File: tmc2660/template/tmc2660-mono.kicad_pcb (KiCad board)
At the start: 4 copper layers, 25 x 40 mm, 19 parts, among them J100 0R, M100 Mount, M101 Mount, P100 Motor, U100 TMC2660

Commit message: Consistently name first block TMC2660-100 in schematic and pcb.
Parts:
- removed REF**: OSHW, Symbols:Symbol_OSHW-Logo_SilkScreen
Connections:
- net /TMC2660-Block/A1 renamed /TMC2660-100/A1
- net /TMC2660-Block/A2 renamed /TMC2660-100/A2
- net /TMC2660-Block/B1 renamed /TMC2660-100/B1
- net /TMC2660-Block/B2 renamed /TMC2660-100/B2
- net /TMC2660-Block/BRA renamed /TMC2660-100/BRA
- net /TMC2660-Block/BRB renamed /TMC2660-100/BRB
- net /TMC2660-Block/CS renamed /TMC2660-100/CS
- net /TMC2660-Block/DIR renamed /TMC2660-100/DIR
- net /TMC2660-Block/GLOBAL_MISO renamed /TMC2660-100/GLOBAL_MISO
- net /TMC2660-Block/MISO renamed /TMC2660-100/MISO
- net /TMC2660-Block/MOSI renamed /TMC2660-100/MOSI
- net /TMC2660-Block/SCLK renamed /TMC2660-100/SCLK
- net /TMC2660-Block/STEP renamed /TMC2660-100/STEP
- net /TMC2660-Block/~EN renamed /TMC2660-100/~EN
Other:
- board text removed: "%%gitversion%%"
- board text removed: "github.com hzeller/quadrigotion"

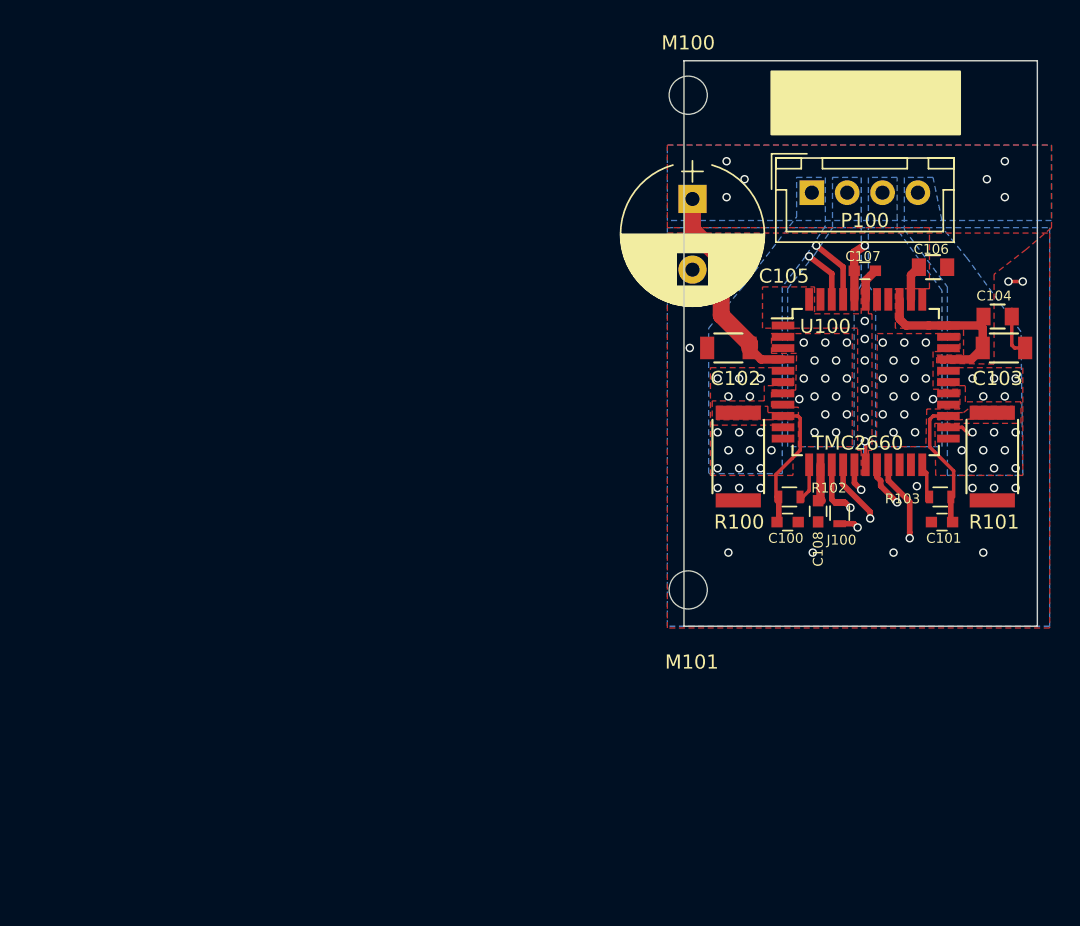
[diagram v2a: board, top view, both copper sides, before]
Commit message: Start with MOSI on the right; turn around board.
- Turn template board upside down, so that the IDC data connector
  can be on the left, and the motor outputs are marked 1..4 seen
  from there.
- Instead of the last chip returning its output, we have it
  receive the MOSI. That way, the leftmost chip is naturally
  number 1 in the sequence of the shift register.
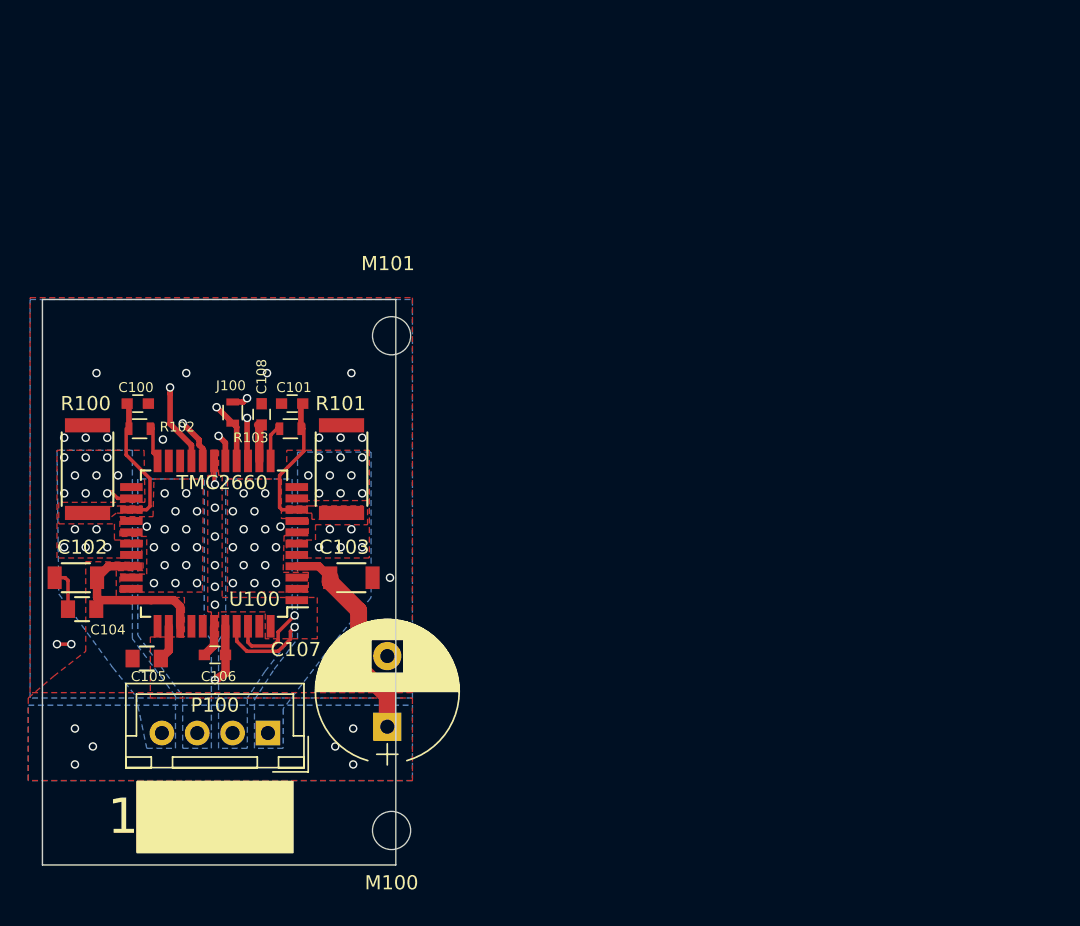
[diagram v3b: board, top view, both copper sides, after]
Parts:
- moved C104 68.0 mm to (74.4, 70.4), turned to 180 degrees
- moved C102 67.6 mm to (74.0, 68.2), turned to 180 degrees
- moved R100 64.0 mm to (74.8, 60.5), turned to 90 degrees
- moved C105 62.1 mm to (79.0, 73.9), turned to 0 degrees
- moved C100 57.5 mm to (78.4, 55.9), turned to 0 degrees
- moved R102 56.8 mm to (78.5, 57.7), turned to 0 degrees
- moved M100 56.1 mm to (96.3, 86.1), turned to 180 degrees
- moved P100 54.2 mm to (87.6, 79.2), turned to 180 degrees
- moved C106 53.4 mm to (83.8, 73.7), turned to 180 degrees
- moved U100 47.5 mm to (83.8, 65.8), turned to 180 degrees
- moved J100 43.5 mm to (85.1, 56.5), turned to 270 degrees
- moved C107 43.1 mm to (96.0, 78.7), turned to 90 degrees
- moved C108 40.0 mm to (87.1, 56.6), turned to 90 degrees
- moved C101 36.0 mm to (89.3, 55.9), turned to 0 degrees
- moved R103 35.6 mm to (89.2, 57.7), turned to 0 degrees
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- renumbered C101 to C100, C100 to C101, C103 to C102, C102 to C103, C106 to C105, C107 to C106, C105 to C107, R101 to R100, R100 to R101, R103 to R102, R102 to R103
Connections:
- net /TMC2660-100/GLOBAL_MISO renamed /TMC2660-100/START_MOSI
- J100 pad 2: /TMC2660-100/MISO -> /TMC2660-100/MOSI
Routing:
- net /TMC2660-100/STEP: track 3.83 -> 5.79 mm
- net /TMC2660-100/DIR: track 4.71 -> 6.48 mm
- net /TMC2660-100/MOSI: track 17.8 -> 17.1 mm
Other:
- board text added: "1"

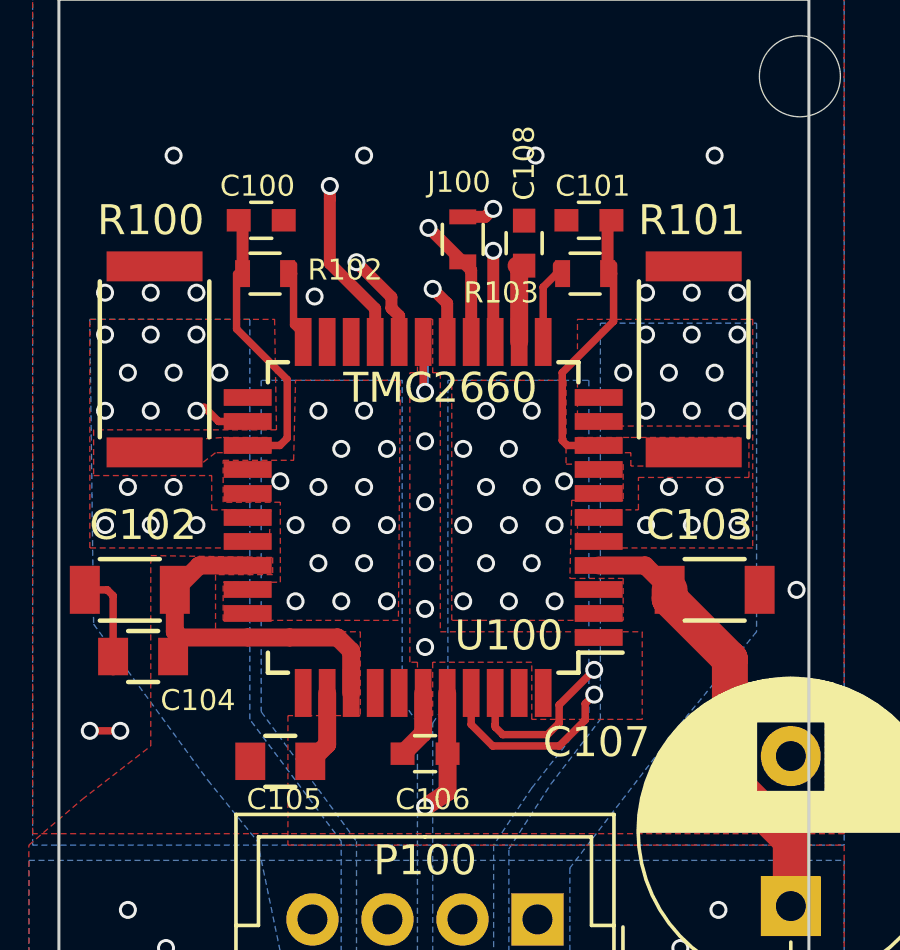
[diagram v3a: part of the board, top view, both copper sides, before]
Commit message: Establish more conservative design rules.
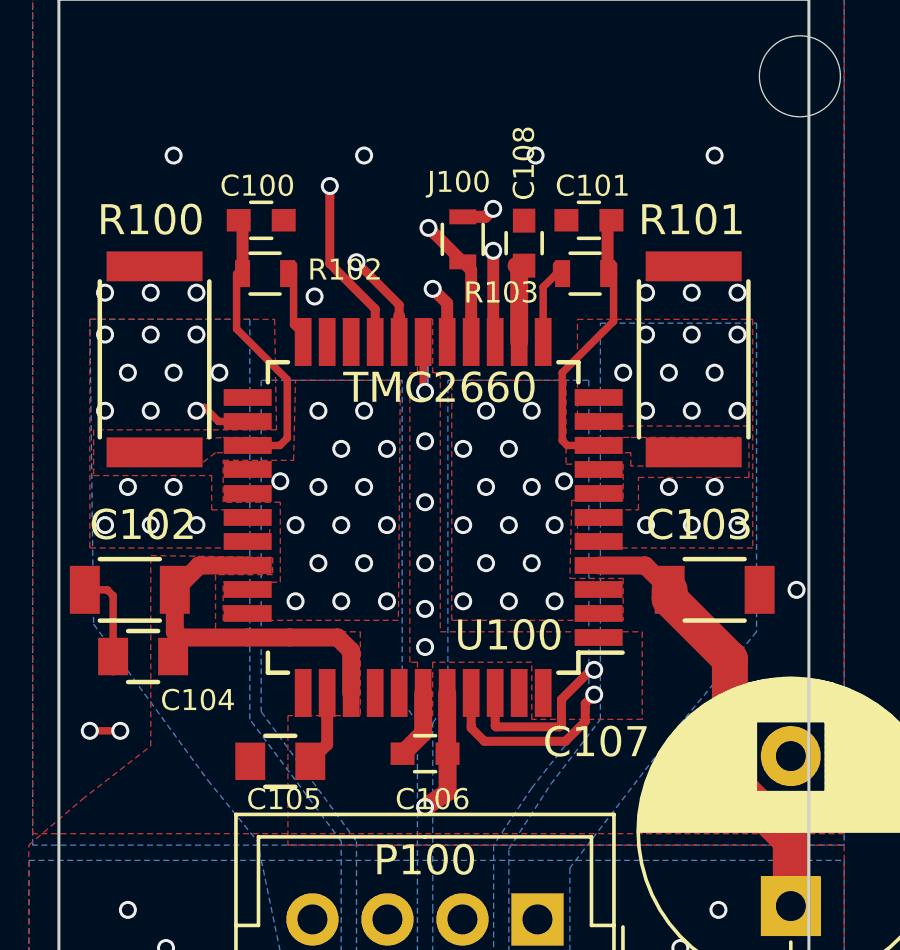
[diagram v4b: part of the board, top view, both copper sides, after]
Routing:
- net /TMC2660-100/CS: track 29.1 -> 30.0 mm
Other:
- net class Default: clearance 0.127 -> 0.18
- net class MotPower: clearance 0.127 -> 0.21
- rule trace_clearance: 0.127 -> 0.18
